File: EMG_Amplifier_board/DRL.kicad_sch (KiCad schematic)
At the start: 4 parts, among them U5 LPV821DBVR, U6 LPV821DBVR

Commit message: add footprints
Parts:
- R15, R16: footprint (none) -> Resistor_SMD:R_0402_1005Metric
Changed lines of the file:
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@@
 	(wire
 		(pts
-			(xy 142.24 85.09) (xy 142.24 88.9)
+			(xy 142.24 57.15) (xy 142.24 88.9)
 		)
 		(stroke
@@
 	(hierarchical_label "V_DD{slash}2"
 		(shape input)
-		(at 142.24 85.09 90)
+		(at 142.24 57.15 90)
 		(fields_autoplaced yes)
 		(effects
@@
 			)
 		)
-		(property "Footprint" ""
+		(property "Footprint" "Resistor_SMD:R_0402_1005Metric"
 			(at 128.27 93.218 90)
 			(effects
@@
 			)
 		)
-		(property "Footprint" ""
+		(property "Footprint" "Resistor_SMD:R_0402_1005Metric"
 			(at 163.83 74.168 90)
 			(effects

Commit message: acomponents choice
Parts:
- R15, R16: footprint Resistor_SMD:R_0402_1005Metric -> Resistor_SMD:R_0201_0603Metric
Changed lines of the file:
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@@
 			)
 		)
-		(property "Footprint" "Resistor_SMD:R_0402_1005Metric"
+		(property "Footprint" "Resistor_SMD:R_0201_0603Metric"
 			(at 128.27 93.218 90)
 			(effects
@@
 			)
 		)
-		(property "Footprint" "Resistor_SMD:R_0402_1005Metric"
+		(property "Footprint" "Resistor_SMD:R_0201_0603Metric"
 			(at 163.83 74.168 90)
 			(effects

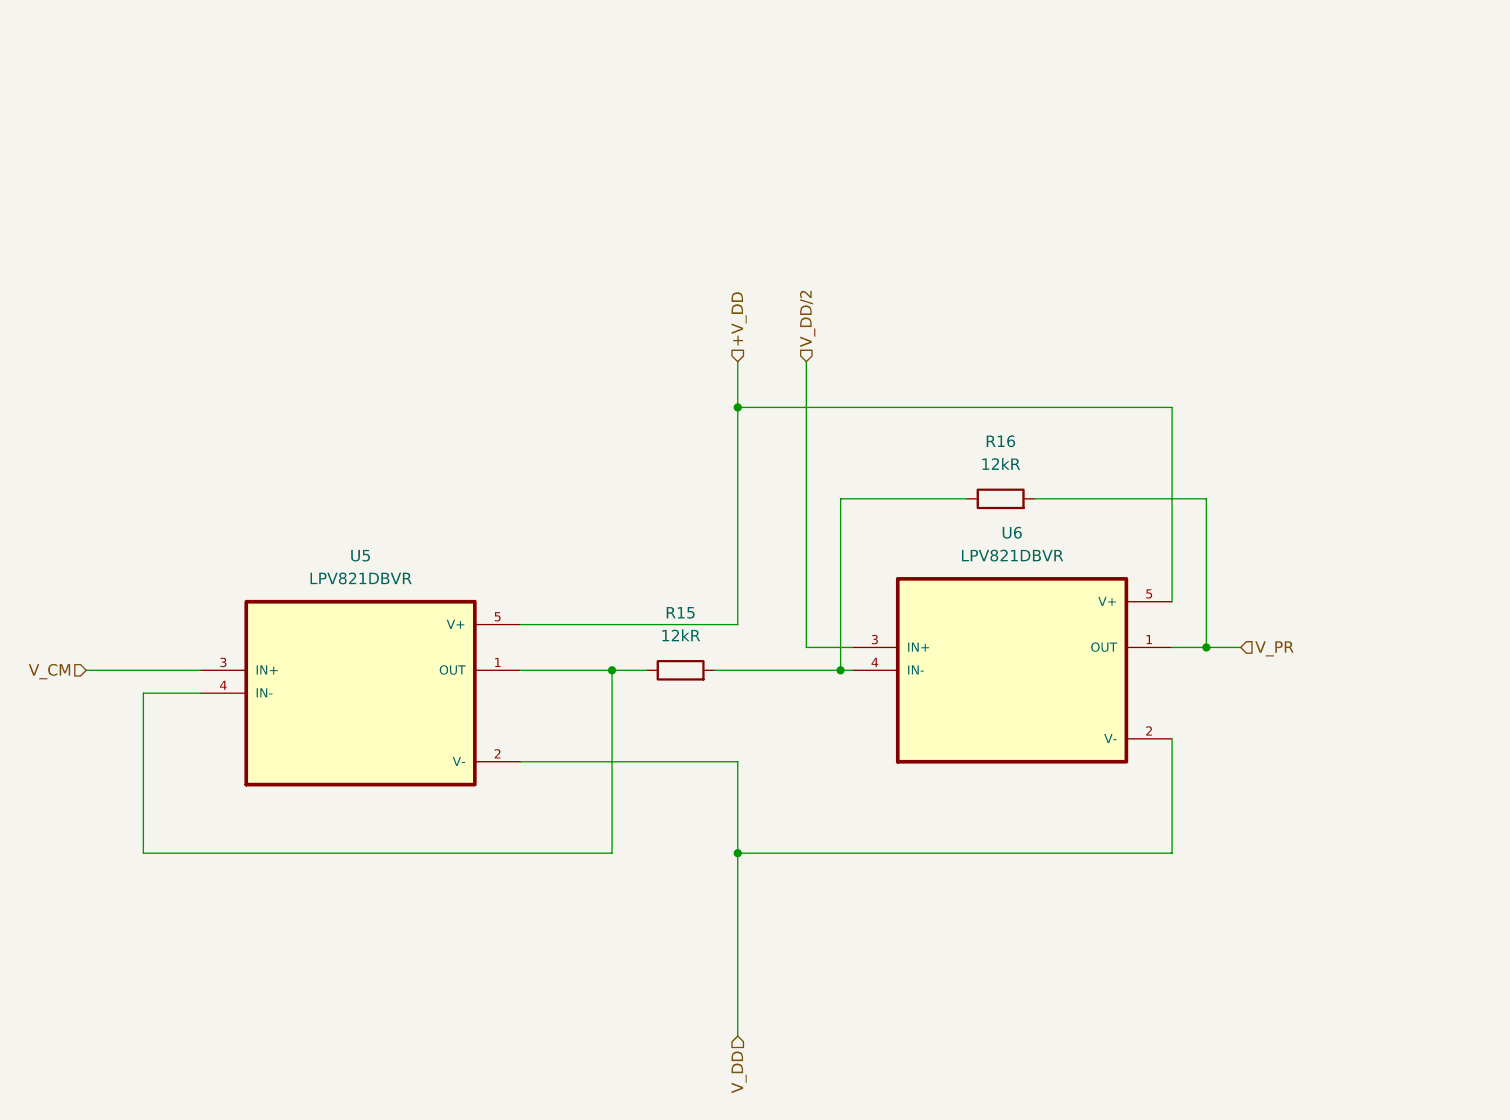
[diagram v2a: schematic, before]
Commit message: update the schematic with shared grounds and pin connectors
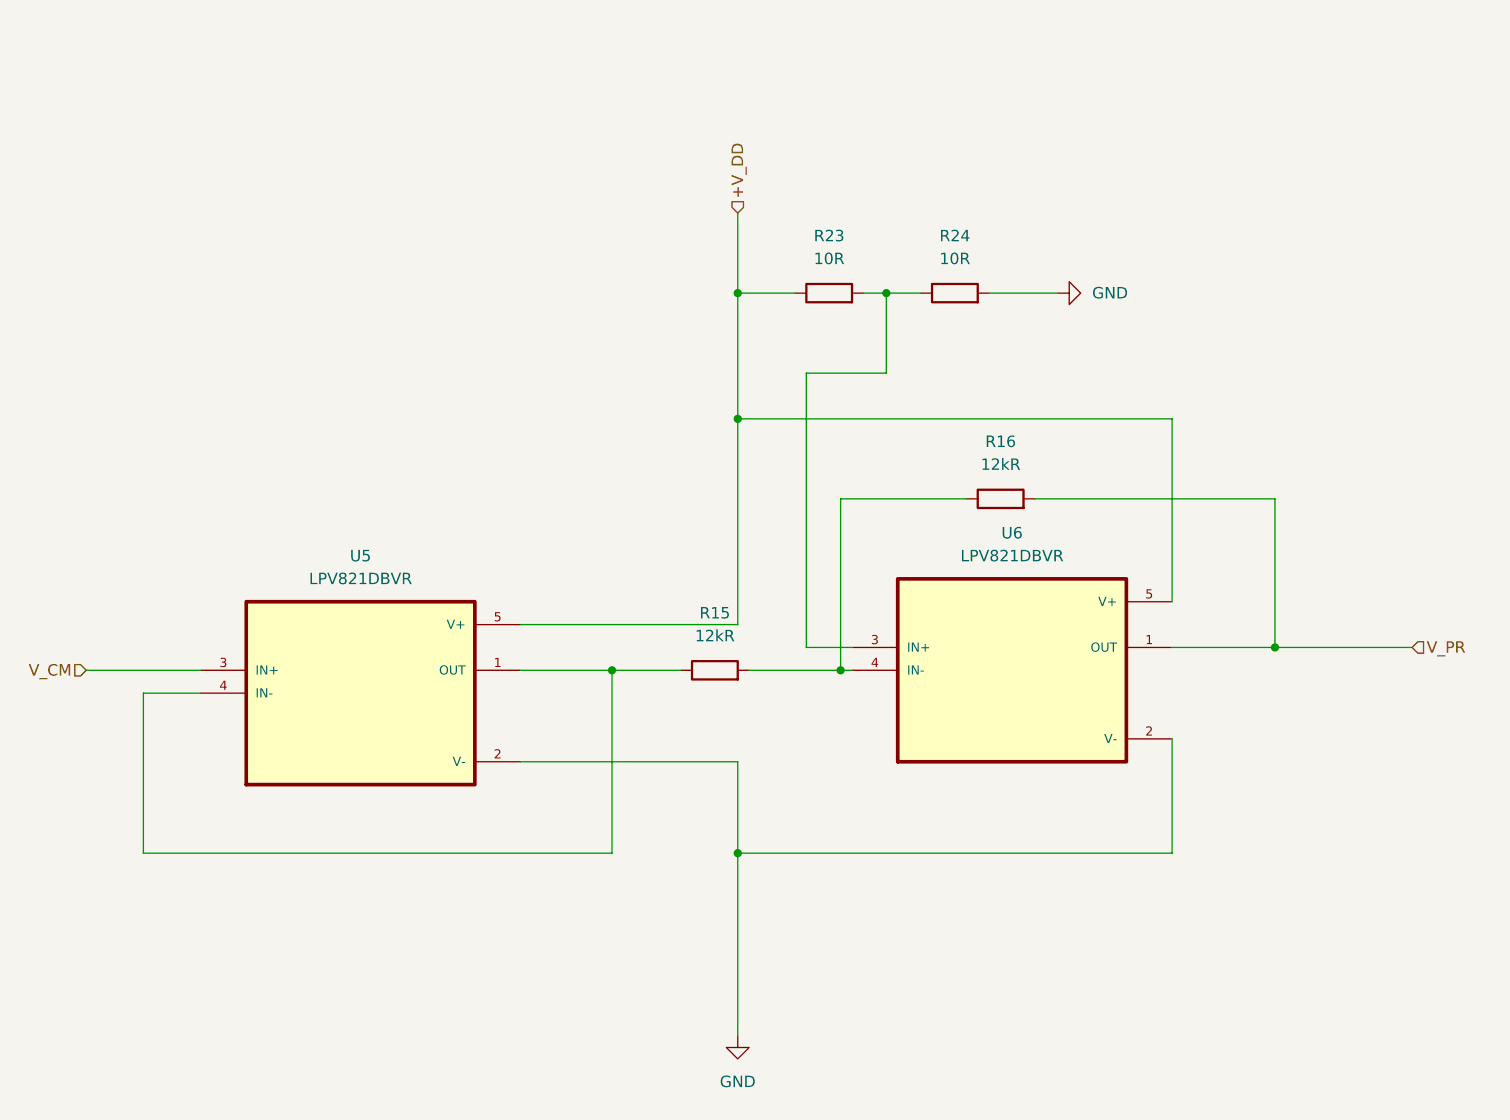
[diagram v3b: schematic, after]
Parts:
- added R23, R24: 10R, Resistor_SMD:R_0402_1005Metric, symbol Device:R
- R15, R16: footprint Resistor_SMD:R_0201_0603Metric -> Resistor_SMD:R_0402_1005Metric
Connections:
- net +V_DD: now also R23.1
- net V_DD renamed GND
- net GND: now also R24.2
- net V_DD/2: no longer names the net of U6.3 (IN+)
- net V_DD/2: now also R23.2, R24.1
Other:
- moved on the sheet: R15

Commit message: pcb design v1
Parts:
- added C12, C8: 0.1uF, Capacitor_SMD:C_0805_2012Metric, symbol Device:C_Small
- R23, R24: value 10R -> 10k
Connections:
- net +V_DD: now also C12.1, C8.1
- net GND: now also C12.2, C8.2

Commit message: first revision
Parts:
- removed C12: 0.1uF, Capacitor_SMD:C_0805_2012Metric, symbol Device:C_Small
- added C9: 0.1uF, Capacitor_SMD:C_0805_2012Metric, symbol Device:C_Small
- R15, R16: value 12kR -> 12k
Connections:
- net +V_DD: now also C9.1
- net GND: now also C9.2
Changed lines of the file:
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@@
+	)
+	(junction
+		(at 134.62 38.1)
+		(diameter 0)
+		(color 0 0 0 0)
 	)
 	(junction
@@
 	)
 	(junction
-		(at 182.88 67.31)
-		(diameter 0)
-		(color 0 0 0 0)
-	)
-	(junction
 		(at 134.62 49.53)
 		(diameter 0)
@@
 	(wire
 		(pts
+			(xy 121.92 38.1) (xy 114.3 38.1)
+		)
+		(stroke
+			(width 0)
+			(type default)
+		)
+	)
+	(wire
+		(pts
 			(xy 134.62 101.6) (xy 110.49 101.6)
 		)
@@
 	(wire
 		(pts
+			(xy 134.62 38.1) (xy 134.62 49.53)
+		)
+		(stroke
+			(width 0)
+			(type default)
+		)
+	)
+	(wire
+		(pts
 			(xy 74.93 93.98) (xy 68.58 93.98)
 		)
@@
 	(wire
 		(pts
-			(xy 195.58 67.31) (xy 203.2 67.31)
-		)
-		(stroke
-			(width 0)
-			(type default)
-		)
-	)
-	(wire
-		(pts
-			(xy 134.62 27.94) (xy 134.62 49.53)
+			(xy 134.62 27.94) (xy 134.62 38.1)
 		)
 		(stroke
@@
 	(wire
 		(pts
-			(xy 190.5 67.31) (xy 182.88 67.31)
-		)
-		(stroke
-			(width 0)
-			(type default)
-		)
-	)
-	(wire
-		(pts
 			(xy 134.62 63.5) (xy 182.88 63.5)
 		)
@@
 	(wire
 		(pts
-			(xy 182.88 63.5) (xy 182.88 67.31)
+			(xy 182.88 63.5) (xy 182.88 83.82)
 		)
 		(stroke
@@
 	(wire
 		(pts
+			(xy 127 38.1) (xy 134.62 38.1)
+		)
+		(stroke
+			(width 0)
+			(type default)
+		)
+	)
+	(wire
+		(pts
 			(xy 151.13 49.53) (xy 154.94 49.53)
 		)
@@
 		(pts
 			(xy 134.62 63.5) (xy 134.62 86.36)
-		)
-		(stroke
-			(width 0)
-			(type default)
-		)
-	)
-	(wire
-		(pts
-			(xy 182.88 67.31) (xy 182.88 83.82)
 		)
 		(stroke
@@
 	(symbol
 		(lib_id "Device:C_Small")
-		(at 193.04 67.31 90)
+		(at 124.46 38.1 270)
 		(unit 1)
 		(exclude_from_sim no)
@@
 		(dnp no)
 		(fields_autoplaced yes)
-		(property "Reference" "C12"
-			(at 193.0463 60.96 90)
+		(property "Reference" "C9"
+			(at 124.4537 44.45 90)
 			(effects
 				(font
@@
 		)
 		(property "Value" "0.1uF"
-			(at 193.0463 63.5 90)
+			(at 124.4537 41.91 90)
 			(effects
 				(font
@@
 		)
 		(property "Footprint" "Capacitor_SMD:C_0805_2012Metric"
-			(at 193.04 67.31 0)
+			(at 124.46 38.1 0)
 			(effects
 				(font
@@
 		)
 		(property "Datasheet" "~"
-			(at 193.04 67.31 0)
+			(at 124.46 38.1 0)
 			(effects
 				(font
@@
 		)
 		(property "Description" "Unpolarized capacitor, small symbol"
-			(at 193.04 67.31 0)
+			(at 124.46 38.1 0)
 			(effects
 				(font
@@
 			(project "EMG_amplifier"
 				(path "/26861adc-1ddf-4c37-9f8b-8db1c0839771/566a5450-97e0-4bc1-8c47-b0ac1397ab98/87e3490f-ae1c-443c-8c09-d2b58f9f3cb7"
-					(reference "C12")
+					(reference "C9")
 					(unit 1)
 				)
@@
 			)
 		)
-		(property "Value" "12kR"
+		(property "Value" "12k"
 			(at 132.08 87.63 90)
 			(effects
@@
 	)
 	(symbol
+		(lib_id "power:GND")
+		(at 114.3 38.1 270)
+		(unit 1)
+		(exclude_from_sim no)
+		(in_bom yes)
+		(on_board yes)
+		(dnp no)
+		(fields_autoplaced yes)
+		(property "Reference" "#PWR013"
+			(at 107.95 38.1 0)
+			(effects
+				(font
+					(size 1.27 1.27)
+				)
+				(hide yes)
+			)
+		)
+		(property "Value" "GND"
+			(at 110.49 38.1001 90)
+			(effects
+				(font
+					(size 1.27 1.27)
+				)
+				(justify right)
+			)
+		)
+		(property "Footprint" ""
+			(at 114.3 38.1 0)
+			(effects
+				(font
+					(size 1.27 1.27)
+				)
+				(hide yes)
+			)
+		)
+		(property "Datasheet" ""
+			(at 114.3 38.1 0)
+			(effects
+				(font
+					(size 1.27 1.27)
+				)
+				(hide yes)
+			)
+		)
+		(property "Description" "Power symbol creates a global label with name \"GND\" , ground"
+			(at 114.3 38.1 0)
+			(effects
+				(font
+					(size 1.27 1.27)
+				)
+				(hide yes)
+			)
+		)
+		(pin "1"
+		)
+		(instances
+			(project "EMG_amplifier"
+				(path "/26861adc-1ddf-4c37-9f8b-8db1c0839771/566a5450-97e0-4bc1-8c47-b0ac1397ab98/87e3490f-ae1c-443c-8c09-d2b58f9f3cb7"
+					(reference "#PWR013")
+					(unit 1)
+				)
+			)
+		)
+	)
+	(symbol
 		(lib_id "Device:R")
 		(at 144.78 49.53 90)
@@
 			)
 		)
-		(property "Value" "12kR"
+		(property "Value" "12k"
 			(at 163.83 68.58 90)
 			(effects
@@
 					(unit 1)
 				)
-			)
-		)
-	)
-	(symbol
-		(lib_id "power:GND")
-		(at 203.2 67.31 90)
-		(unit 1)
-		(exclude_from_sim no)
-		(in_bom yes)
-		(on_board yes)
-		(dnp no)
-		(fields_autoplaced yes)
-		(property "Reference" "#PWR023"
-			(at 209.55 67.31 0)
-			(effects
-				(font
-					(size 1.27 1.27)
-				)
-				(hide yes)
-			)
-		)
-		(property "Value" "GND"
-			(at 207.01 67.3099 90)
-			(effects
-				(font
-					(size 1.27 1.27)
-				)
-				(justify right)
-			)
-		)
-		(property "Footprint" ""
-			(at 203.2 67.31 0)
-			(effects
-				(font
-					(size 1.27 1.27)
-				)
-				(hide yes)
-			)
-		)
-		(property "Datasheet" ""
-			(at 203.2 67.31 0)
-			(effects
-				(font
-					(size 1.27 1.27)
-				)
-				(hide yes)
-			)
-		)
-		(property "Description" "Power symbol creates a global label with name \"GND\" , ground"
-			(at 203.2 67.31 0)
-			(effects
-				(font
-					(size 1.27 1.27)
-				)
-				(hide yes)
-			)
-		)
-		(pin "1"
-		)
-		(instances
-			(project "EMG_amplifier"
-				(path "/26861adc-1ddf-4c37-9f8b-8db1c0839771/566a5450-97e0-4bc1-8c47-b0ac1397ab98/87e3490f-ae1c-443c-8c09-d2b58f9f3cb7"
-					(reference "#PWR023")
-					(unit 1)
-				)

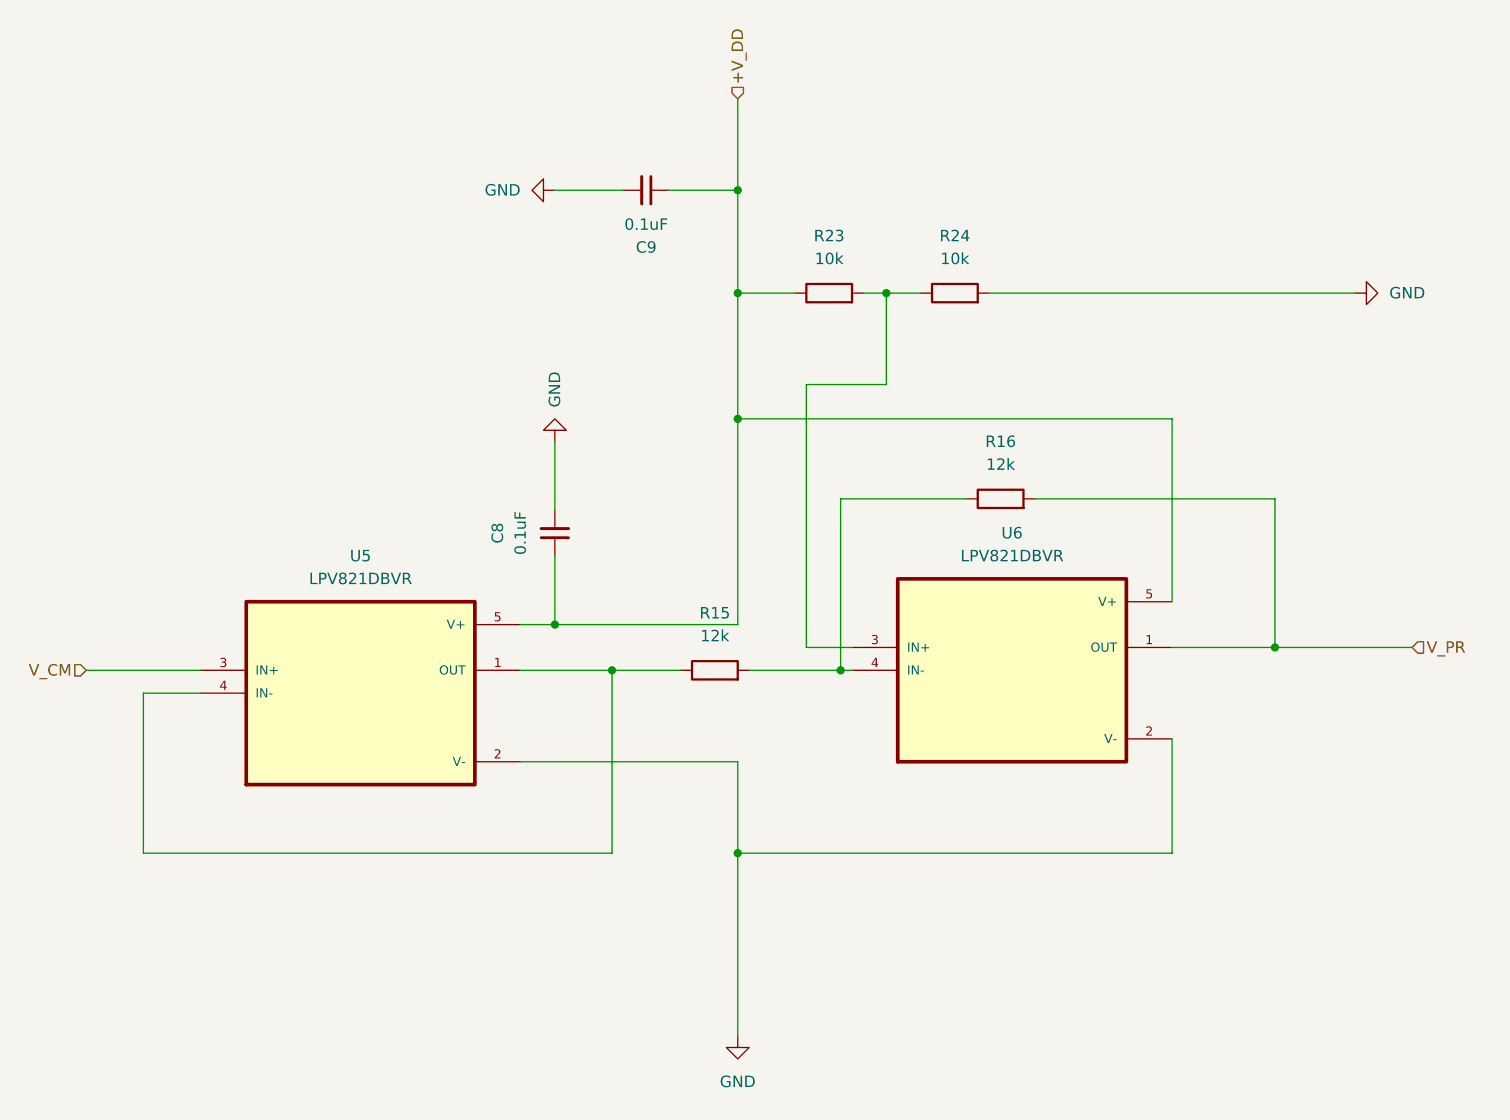
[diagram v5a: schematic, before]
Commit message: center the pin connectors
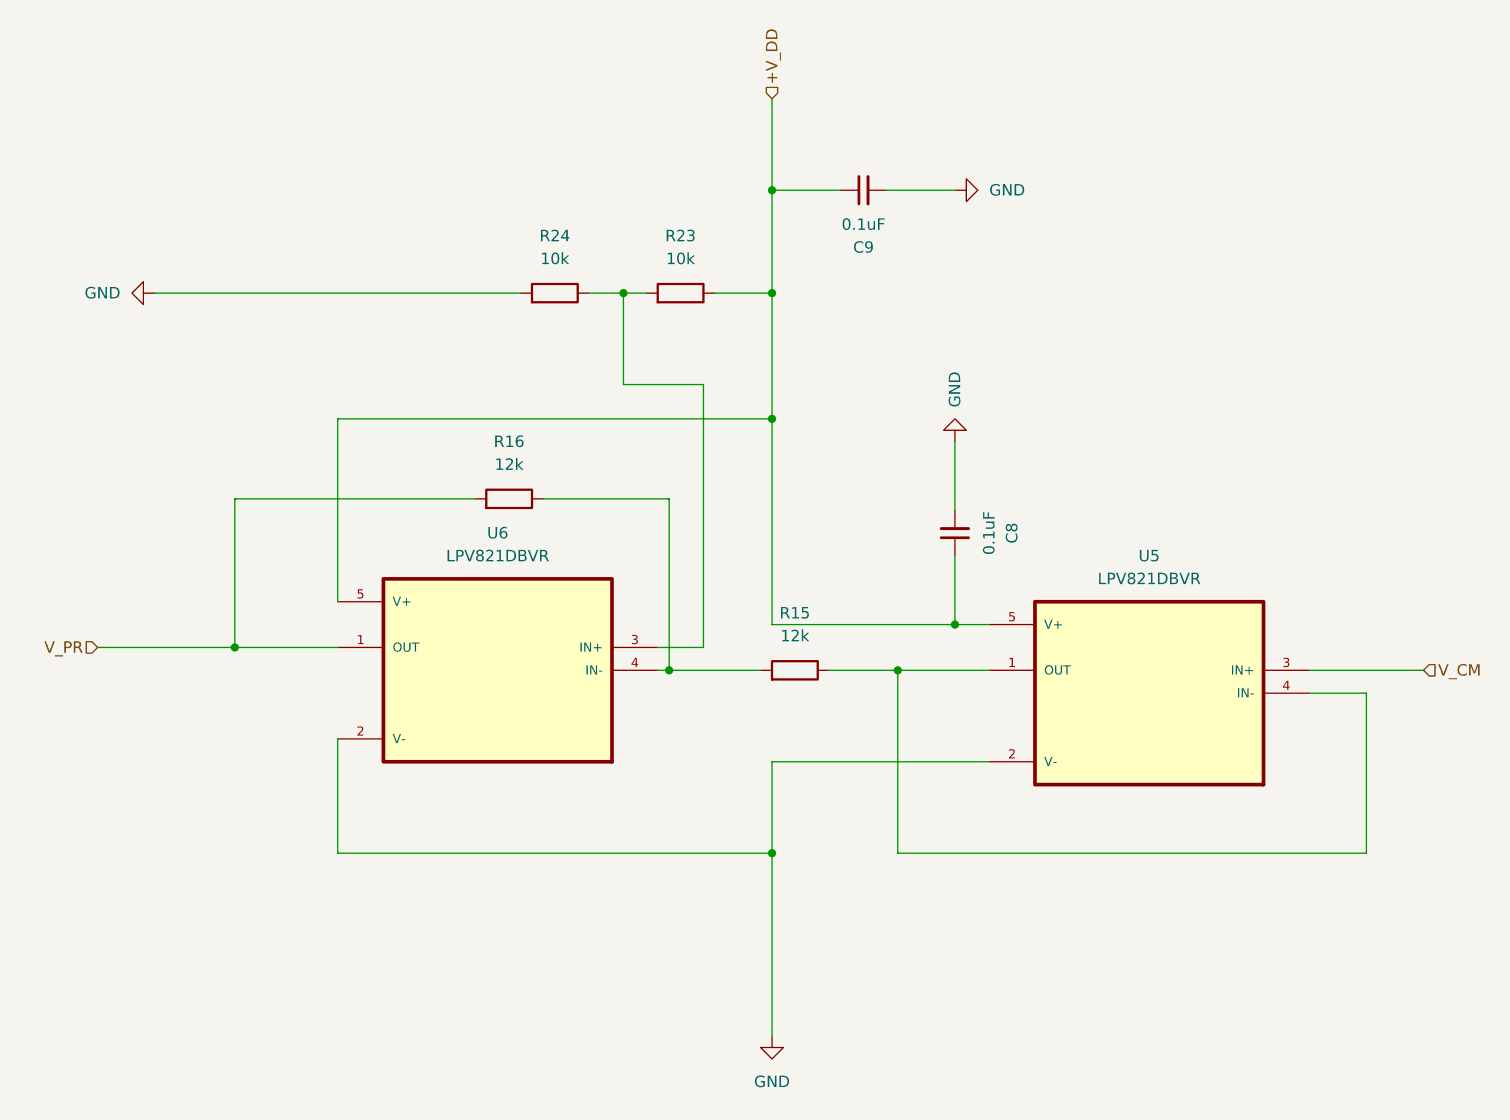
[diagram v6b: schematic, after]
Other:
- moved on the sheet: C8, C9, R15, R16, R23, R24, U5, U6
